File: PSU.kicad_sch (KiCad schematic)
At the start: 85 parts, among them J17 Barrel_Jack_Switch, J18 USB_C_Receptacle_USB2.0_16P, Q7 AON7262E, Q78 2N7002, Q79 2N7002, Q8 2N7002, SW1 SW_Push, SW2 SW_Push, U14 CH224K, U15 LM2734X, U16 LM2734X, U79 TL431DBZ

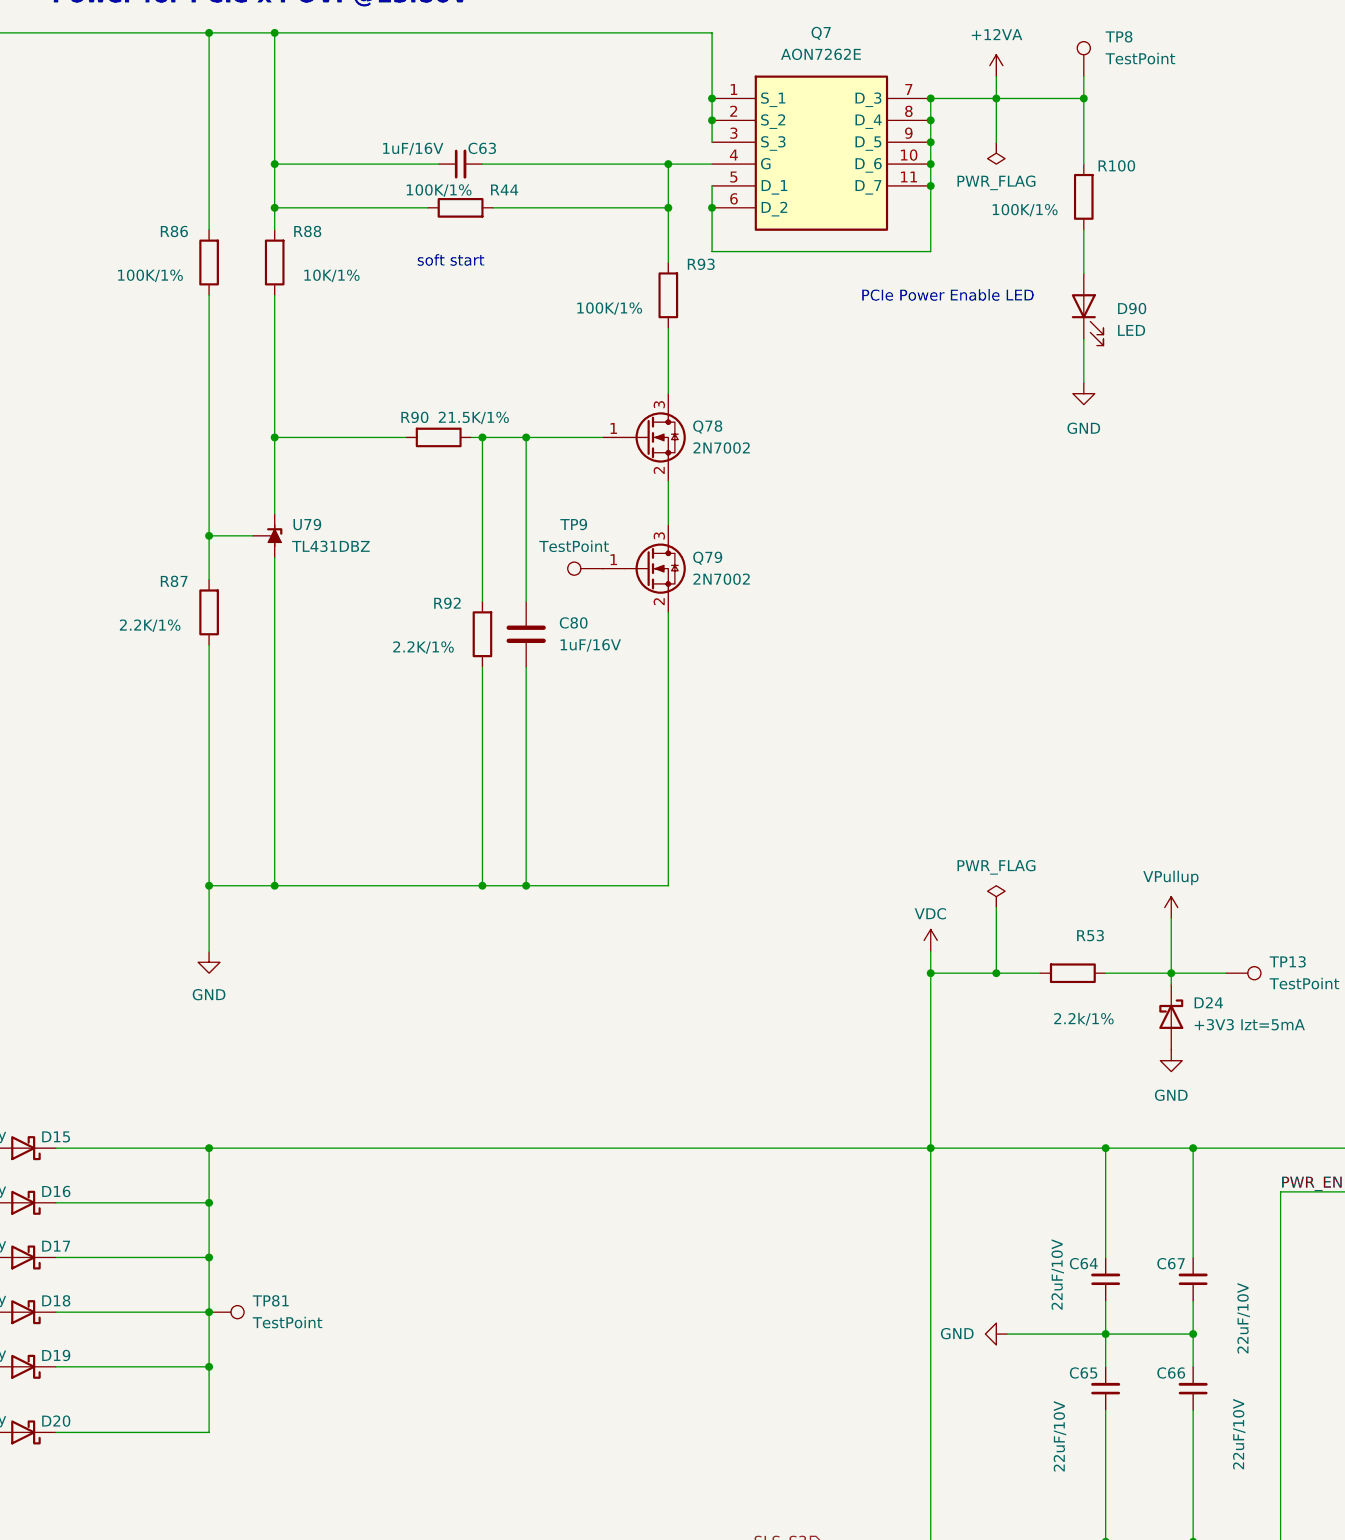
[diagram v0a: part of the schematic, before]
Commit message: Resolved some duplicate annotations
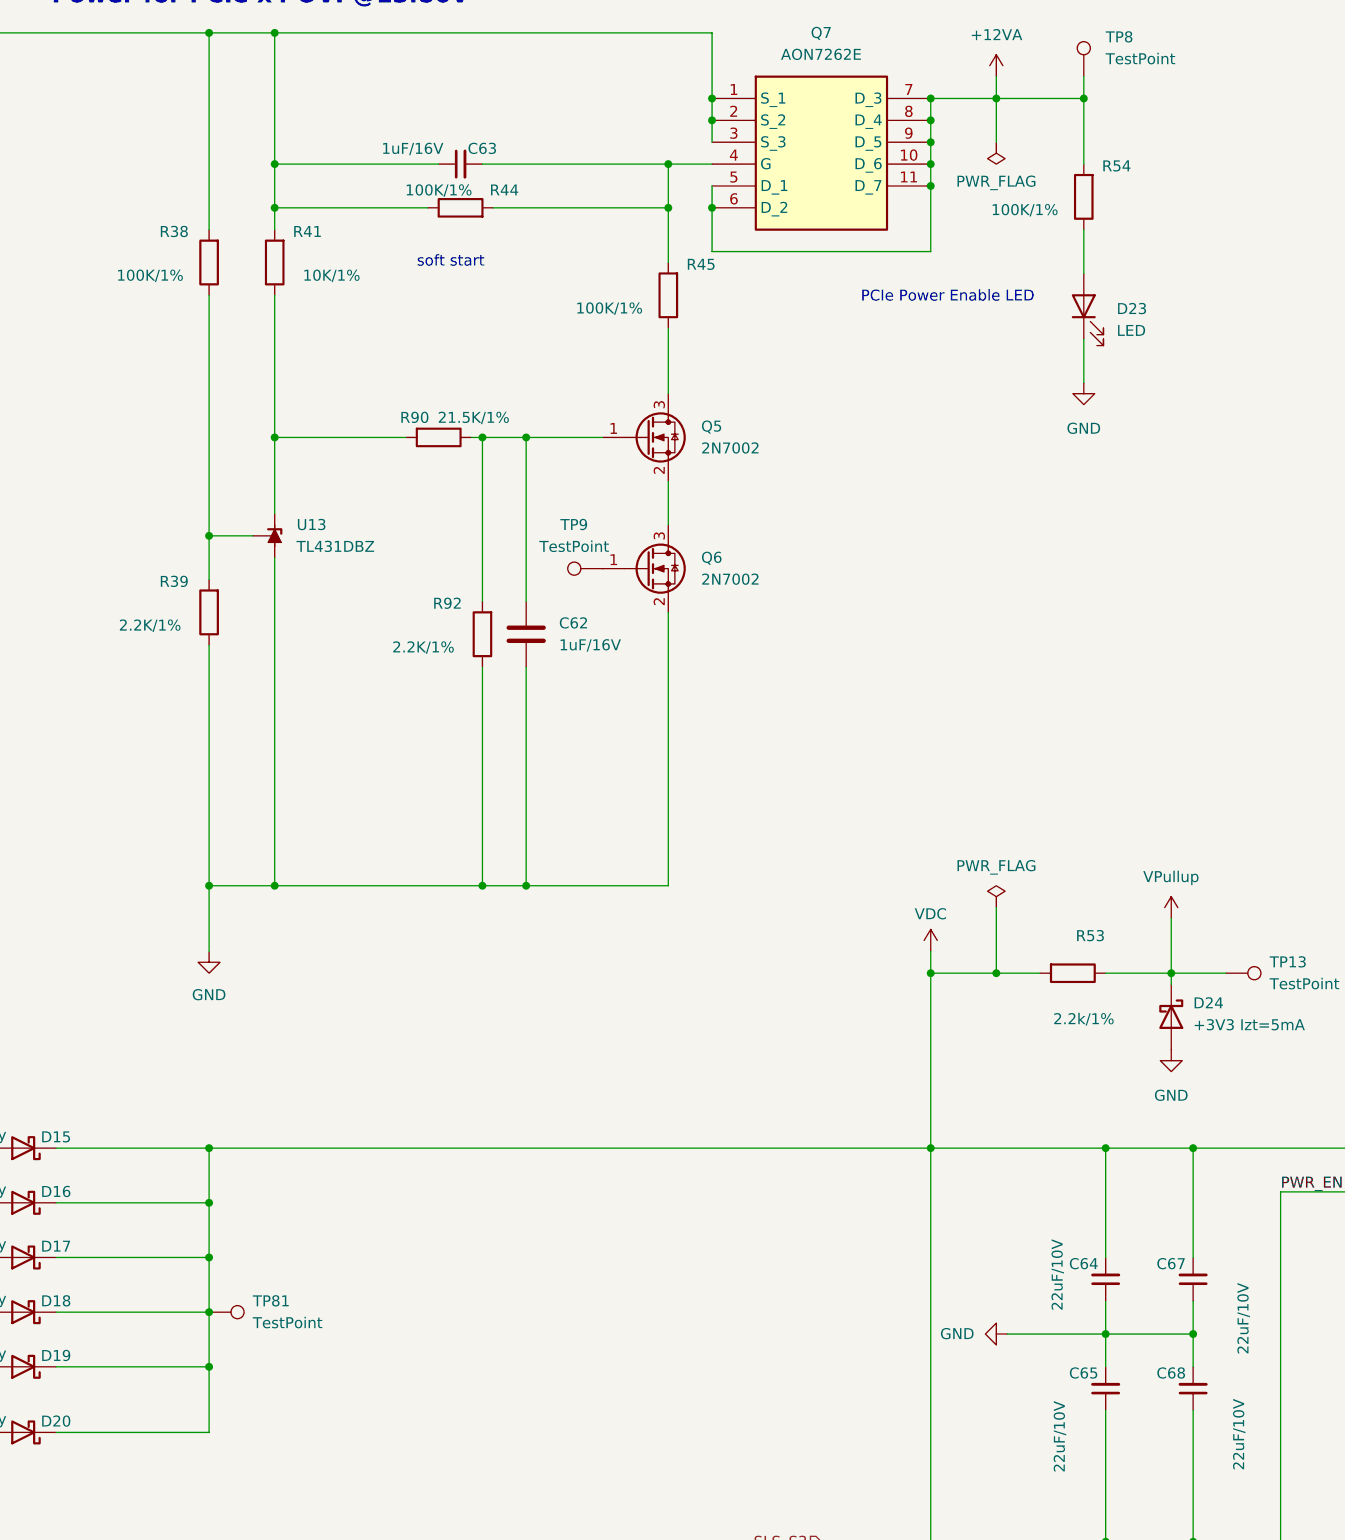
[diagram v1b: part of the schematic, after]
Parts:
- renumbered C80 to C62, C66 to C68, D90 to D23, Q78 to Q5, Q79 to Q6, R86 to R38, R87 to R39, R88 to R41, R93 to R45, R100 to R54, U79 to U13
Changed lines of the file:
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@@
 		(in_pos_files yes)
 		(dnp no)
-		(property "Reference" "R100"
+		(property "Reference" "R54"
 			(at 306.07 78.994 0)
 			(show_name no)
@@
 			(project "Carrier_Board"
 				(path "/e768274e-12f3-4f83-96f6-abb7638e0bc1/a1e78f2f-f14b-4628-9612-5b4e596f5f9f"
-					(reference "R100")
+					(reference "R54")
 					(unit 1)
 				)
@@
 		(dnp no)
 		(fields_autoplaced yes)
-		(property "Reference" "U79"
-			(at 210.312 120.6499 90)
+		(property "Reference" "U13"
+			(at 210.82 120.6499 90)
 			(show_name no)
 			(do_not_autoplace no)
@@
 		)
 		(property "Value" "TL431DBZ"
-			(at 210.312 123.1899 90)
+			(at 210.82 123.1899 90)
 			(show_name no)
 			(do_not_autoplace no)
@@
 			(project "Carrier_Board"
 				(path "/e768274e-12f3-4f83-96f6-abb7638e0bc1/a1e78f2f-f14b-4628-9612-5b4e596f5f9f"
-					(reference "U79")
+					(reference "U13")
 					(unit 1)
 				)
@@
 		(dnp no)
 		(fields_autoplaced yes)
-		(property "Reference" "Q79"
-			(at 256.794 124.4599 0)
+		(property "Reference" "Q6"
+			(at 257.81 124.4599 0)
 			(show_name no)
 			(do_not_autoplace no)
@@
 		)
 		(property "Value" "2N7002"
-			(at 256.794 126.9999 0)
+			(at 257.81 126.9999 0)
 			(show_name no)
 			(do_not_autoplace no)
@@
 			(project "Carrier_Board"
 				(path "/e768274e-12f3-4f83-96f6-abb7638e0bc1/a1e78f2f-f14b-4628-9612-5b4e596f5f9f"
-					(reference "Q79")
+					(reference "Q6")
 					(unit 1)
 				)
@@
 		(in_pos_files yes)
 		(dnp no)
-		(property "Reference" "R88"
+		(property "Reference" "R41"
 			(at 212.09 86.614 0)
 			(show_name no)
@@
 			(project "Carrier_Board"
 				(path "/e768274e-12f3-4f83-96f6-abb7638e0bc1/a1e78f2f-f14b-4628-9612-5b4e596f5f9f"
-					(reference "R88")
+					(reference "R41")
 					(unit 1)
 				)
@@
 		(in_pos_files yes)
 		(dnp no)
-		(property "Reference" "R93"
+		(property "Reference" "R45"
 			(at 257.81 90.424 0)
 			(show_name no)
@@
 			(project "Carrier_Board"
 				(path "/e768274e-12f3-4f83-96f6-abb7638e0bc1/a1e78f2f-f14b-4628-9612-5b4e596f5f9f"
-					(reference "R93")
+					(reference "R45")
 					(unit 1)
 				)
@@
 		(in_pos_files yes)
 		(dnp no)
-		(property "Reference" "C66"
+		(property "Reference" "C68"
 			(at 312.42 219.202 0)
 			(show_name no)
@@
 			(project "Carrier_Board"
 				(path "/e768274e-12f3-4f83-96f6-abb7638e0bc1/a1e78f2f-f14b-4628-9612-5b4e596f5f9f"
-					(reference "C66")
+					(reference "C68")
 					(unit 1)
 				)
@@
 		(dnp no)
 		(fields_autoplaced yes)
-		(property "Reference" "D90"
+		(property "Reference" "D23"
 			(at 306.07 95.5674 90)
 			(show_name no)
@@
 			(project "Carrier_Board"
 				(path "/e768274e-12f3-4f83-96f6-abb7638e0bc1/a1e78f2f-f14b-4628-9612-5b4e596f5f9f"
-					(reference "D90")
+					(reference "D23")
 					(unit 1)
 				)
@@
 		(dnp no)
 		(fields_autoplaced yes)
-		(property "Reference" "C80"
+		(property "Reference" "C62"
 			(at 241.3 132.0799 0)
 			(show_name no)
@@
 			(project "Carrier_Board"
 				(path "/e768274e-12f3-4f83-96f6-abb7638e0bc1/a1e78f2f-f14b-4628-9612-5b4e596f5f9f"
-					(reference "C80")
+					(reference "C62")
 					(unit 1)
 				)
@@
 		(in_pos_files yes)
 		(dnp no)
-		(property "Reference" "R87"
+		(property "Reference" "R39"
 			(at 196.596 127.254 0)
 			(show_name no)
@@
 			(project "Carrier_Board"
 				(path "/e768274e-12f3-4f83-96f6-abb7638e0bc1/a1e78f2f-f14b-4628-9612-5b4e596f5f9f"
-					(reference "R87")
+					(reference "R39")
 					(unit 1)
 				)
@@
 		(dnp no)
 		(fields_autoplaced yes)
-		(property "Reference" "Q78"
-			(at 256.794 109.2199 0)
+		(property "Reference" "Q5"
+			(at 257.81 109.2199 0)
 			(show_name no)
 			(do_not_autoplace no)
@@
 		)
 		(property "Value" "2N7002"
-			(at 256.794 111.7599 0)
+			(at 257.81 111.7599 0)
 			(show_name no)
 			(do_not_autoplace no)
@@
 			(project "Carrier_Board"
 				(path "/e768274e-12f3-4f83-96f6-abb7638e0bc1/a1e78f2f-f14b-4628-9612-5b4e596f5f9f"
-					(reference "Q78")
+					(reference "Q5")
 					(unit 1)
 				)
@@
 		(in_pos_files yes)
 		(dnp no)
-		(property "Reference" "R86"
+		(property "Reference" "R38"
 			(at 196.596 86.614 0)
 			(show_name no)
@@
 			(project "Carrier_Board"
 				(path "/e768274e-12f3-4f83-96f6-abb7638e0bc1/a1e78f2f-f14b-4628-9612-5b4e596f5f9f"
-					(reference "R86")
+					(reference "R38")
 					(unit 1)
 				)

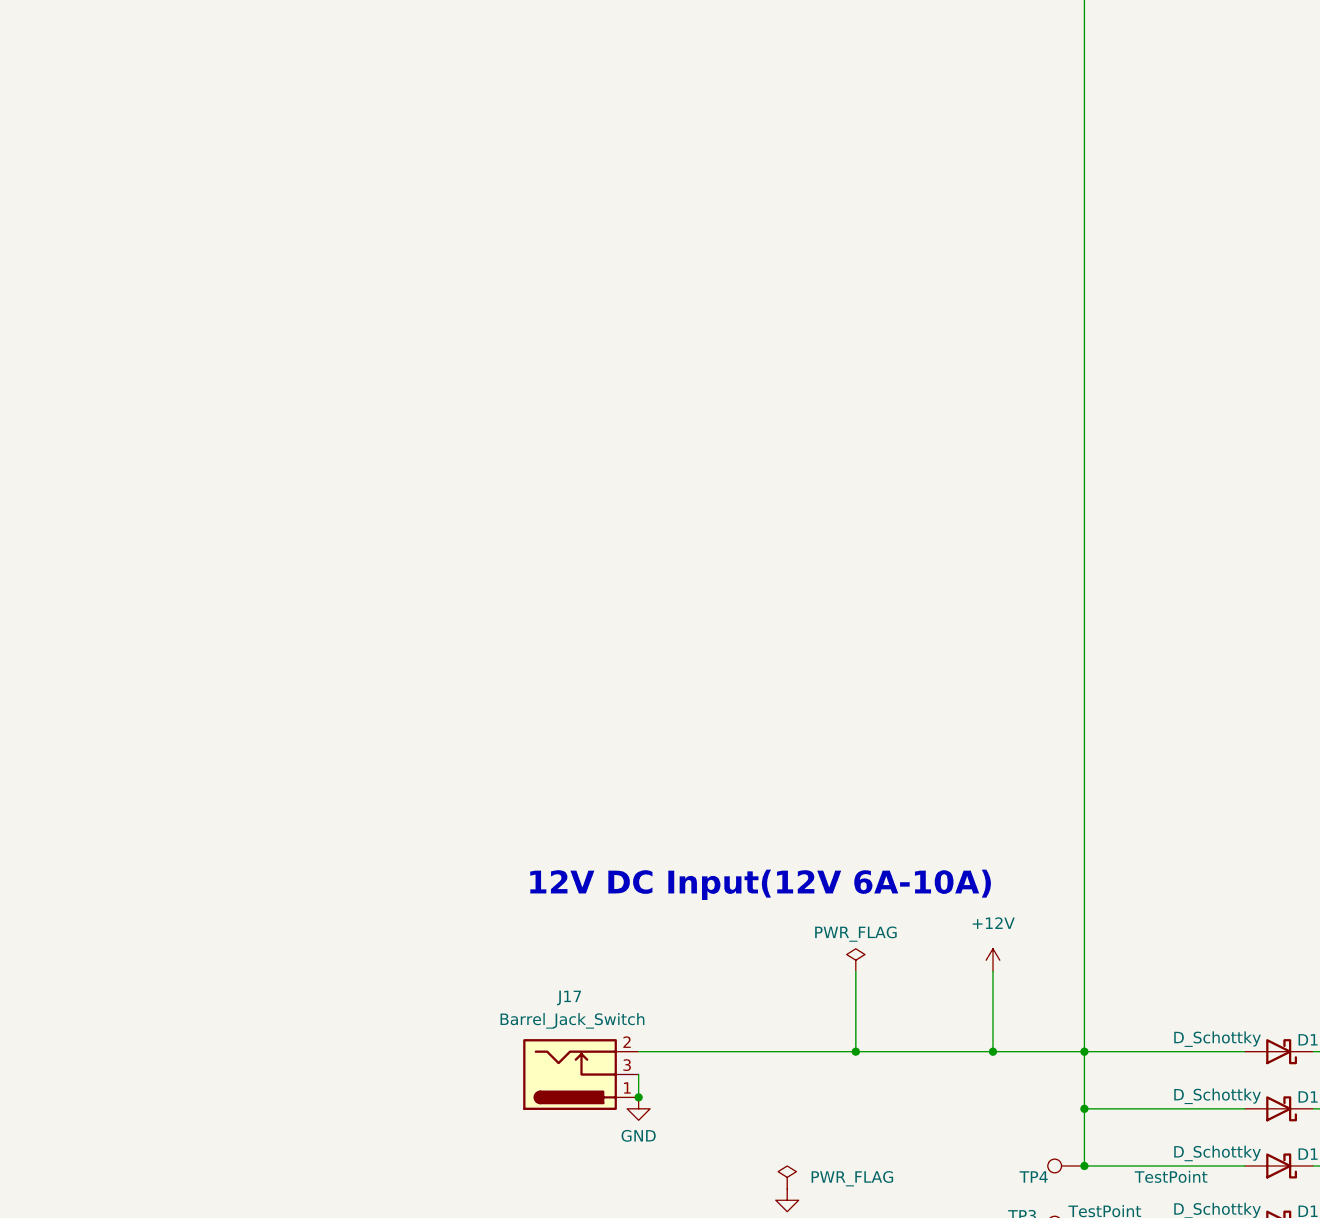
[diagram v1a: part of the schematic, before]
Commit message: Added power supply connector to interface directly with external power supply molex connetcor
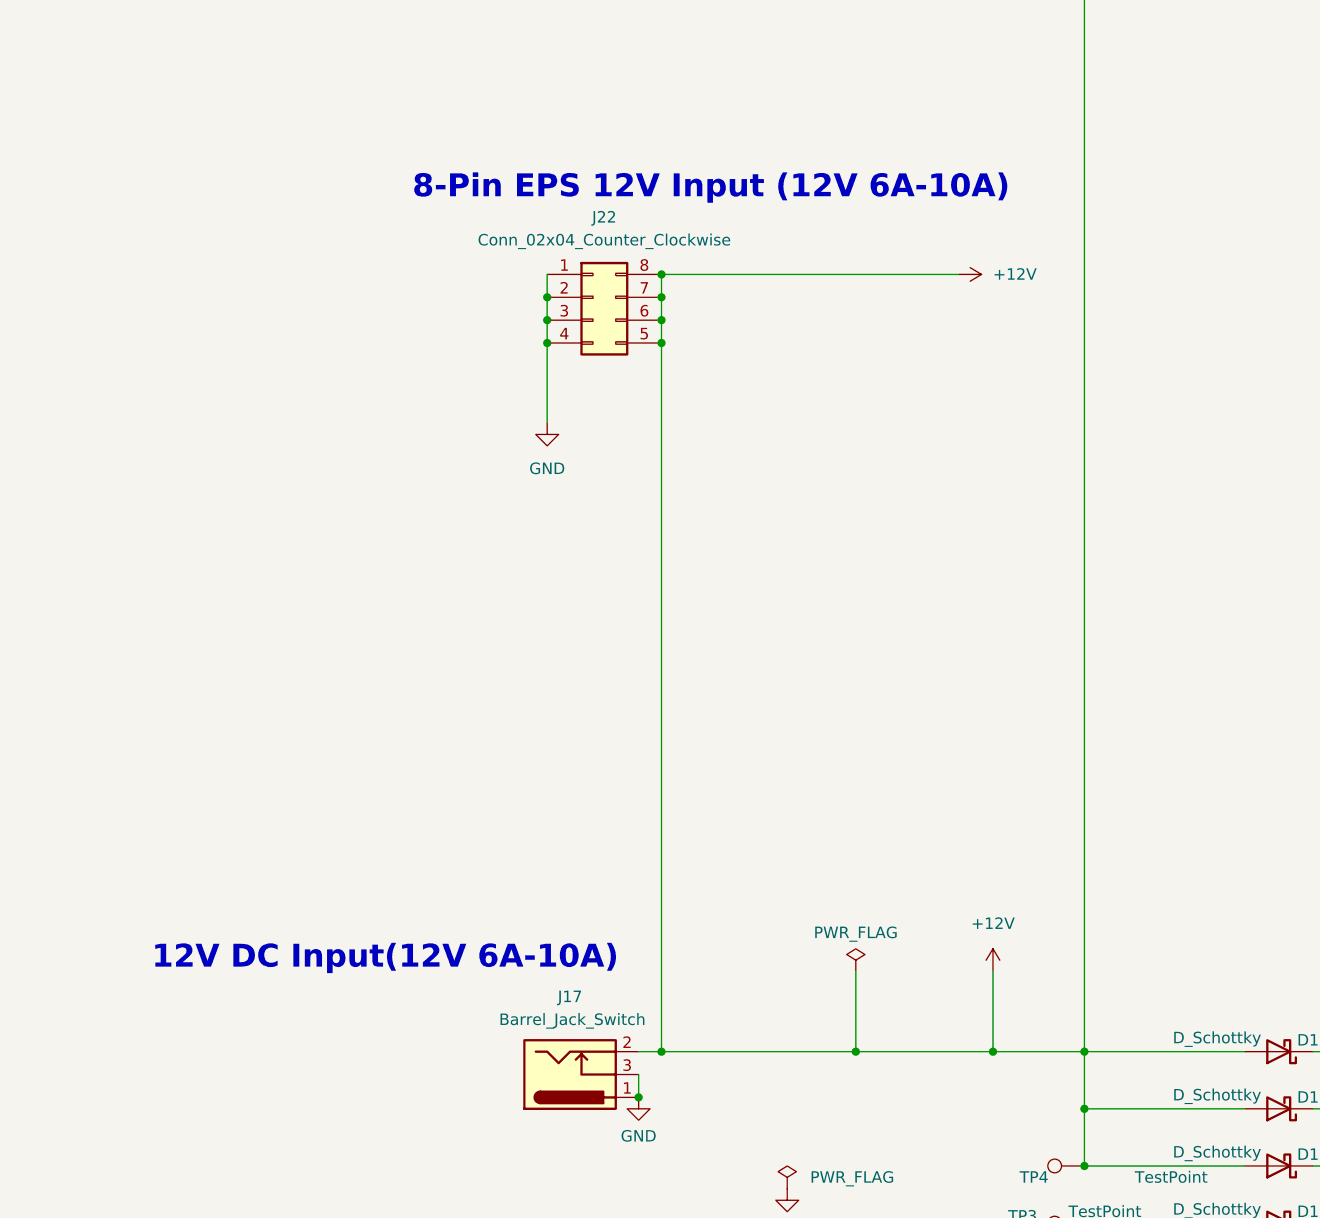
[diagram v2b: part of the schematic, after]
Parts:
- added J22: Conn_02x04_Counter_Clockwise, Custom_Connectors:CONN_5569-08A_MOL, symbol Connector_Generic:Conn_02x04_Counter_Clockwise
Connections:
- net +12V: now also J22.5 (Pin_5), J22.6 (Pin_6), J22.7 (Pin_7), J22.8 (Pin_8)
- net GND: now also J22.1 (Pin_1), J22.2 (Pin_2), J22.3 (Pin_3), J22.4 (Pin_4)
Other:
- note added: "8-Pin EPS 12V Input (12V 6A-10A)"
